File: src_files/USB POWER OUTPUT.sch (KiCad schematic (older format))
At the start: 28 parts, among them J1 USB_A, J10 USB_A, J11 USB_A, J12 USB_A, U22 SY6280AAAC, U23 SY6280AAAC, U24 SY6280AAAC, U25 SY6280AAAC

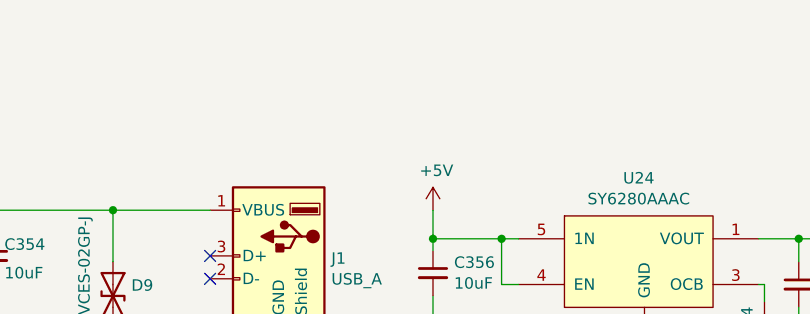
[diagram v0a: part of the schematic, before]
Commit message: added usb power output
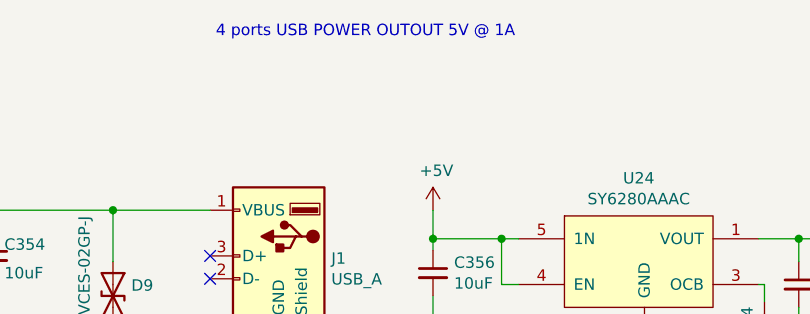
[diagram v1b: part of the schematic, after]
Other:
- note added: "4 ports USB POWER OUTOUT 5V @ 1A"
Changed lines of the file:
@@
 	1    0    0    -1
 $EndComp
+Text Notes 4775 1375 0    50   ~ 0
+4 ports USB POWER OUTOUT 5V @ 1A
 $EndSCHEMATC

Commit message: updates rules check and associations
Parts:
- R122, R123, R124, R125: footprint (none) -> Resistor_SMD:R_0402_1005Metric
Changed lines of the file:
@@
 $Descr A4 11693 8268
 encoding utf-8
-Sheet 17 17
+Sheet 16 17
 Title ""
 Date ""
@@
 F 0 "R122" V 3175 2500 50  0000 L CNN
 F 1 "6.8K" V 3325 2475 50  0000 L CNN
-F 2 "" V 3290 2540 50  0001 C CNN
+F 2 "Resistor_SMD:R_0402_1005Metric" V 3290 2540 50  0001 C CNN
 F 3 "~" H 3250 2550 50  0001 C CNN
 	1    3250 2550
@@
 F 0 "R123" V 3175 4625 50  0000 L CNN
 F 1 "6.8K" V 3325 4600 50  0000 L CNN
-F 2 "" V 3290 4665 50  0001 C CNN
+F 2 "Resistor_SMD:R_0402_1005Metric" V 3290 4665 50  0001 C CNN
 F 3 "~" H 3250 4675 50  0001 C CNN
 	1    3250 4675
@@
 F 0 "R124" V 7100 2625 50  0000 L CNN
 F 1 "6.8K" V 7250 2600 50  0000 L CNN
-F 2 "" V 7215 2665 50  0001 C CNN
+F 2 "Resistor_SMD:R_0402_1005Metric" V 7215 2665 50  0001 C CNN
 F 3 "~" H 7175 2675 50  0001 C CNN
 	1    7175 2675
@@
 F 0 "R125" V 7200 4650 50  0000 L CNN
 F 1 "6.8K" V 7350 4625 50  0000 L CNN
-F 2 "" V 7315 4690 50  0001 C CNN
+F 2 "Resistor_SMD:R_0402_1005Metric" V 7315 4690 50  0001 C CNN
 F 3 "~" H 7275 4700 50  0001 C CNN
 	1    7275 4700

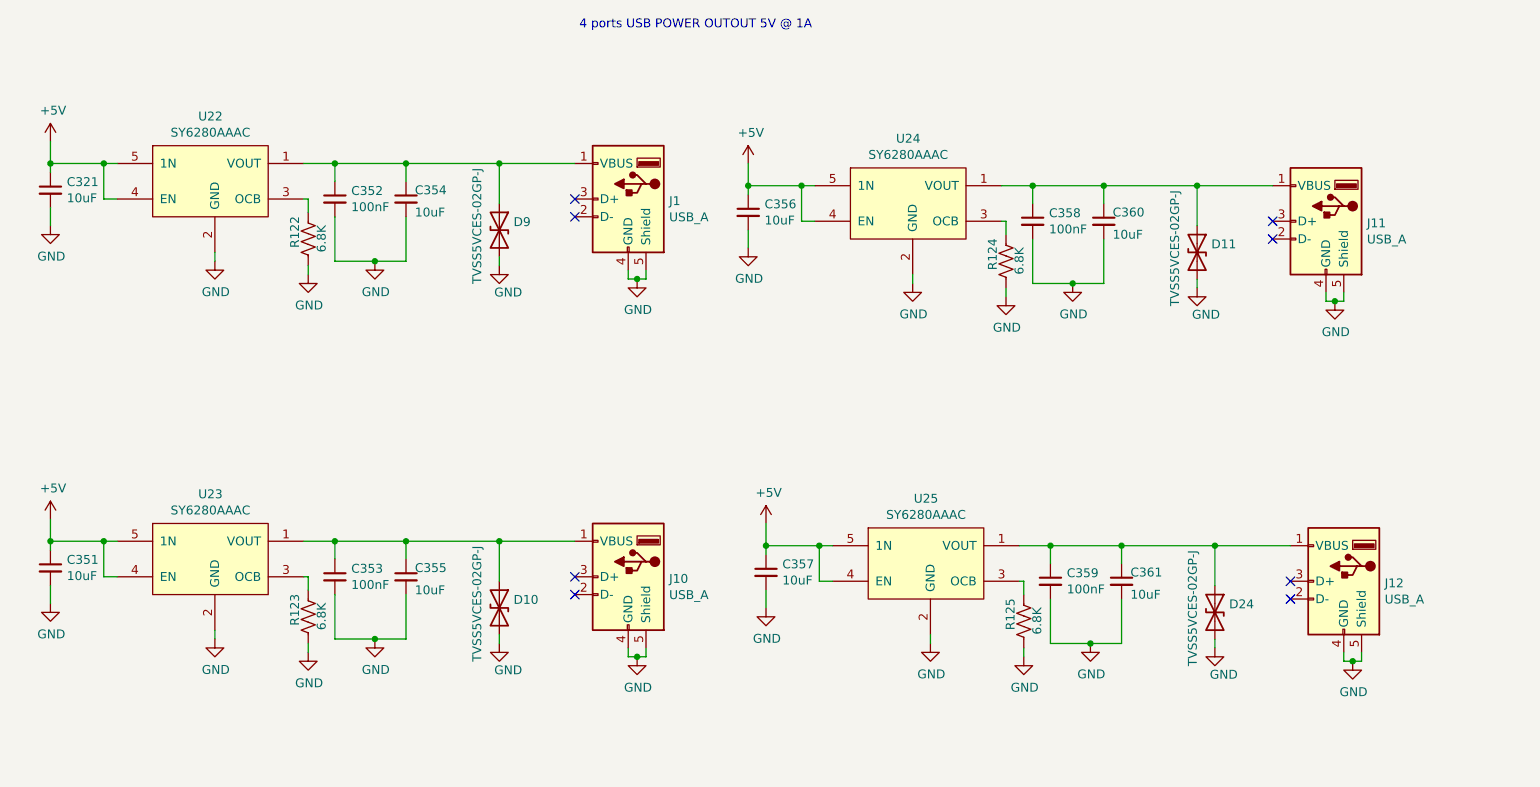
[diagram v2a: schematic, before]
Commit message: update schematic
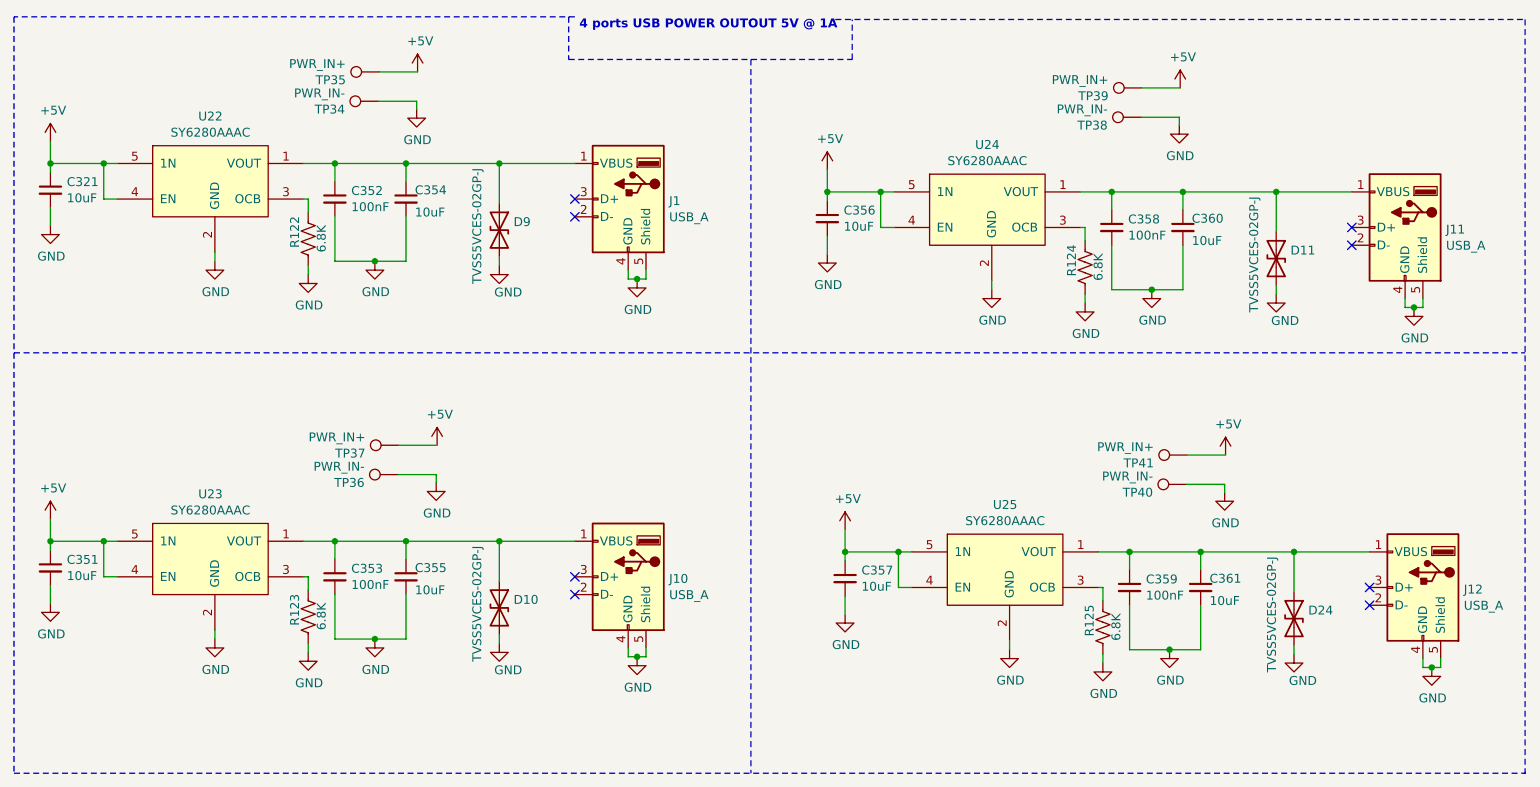
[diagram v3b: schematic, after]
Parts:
- added TP34, TP36, TP38, TP40: PWR_IN-, TestPoint:TestPoint_Pad_2.0x2.0mm, symbol Connector:TestPoint
- added TP35, TP37, TP39, TP41: PWR_IN+, TestPoint:TestPoint_Pad_2.0x2.0mm, symbol Connector:TestPoint
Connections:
- net +5V: now also TP35.1, TP37.1, TP39.1, TP41.1
- net GND: now also TP34.1, TP36.1, TP38.1, TP40.1
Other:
- moved on the sheet: C356, C357, C358, C359, C360, C361, D11, D24, J11, J12, R124, R125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
